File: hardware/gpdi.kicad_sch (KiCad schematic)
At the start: 11 parts, among them J1 GPDI_A, Q1 BSN20, U14 UCL0524P, U15 UCL0524P

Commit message: Initial layout
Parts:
- R21: renamed from R16; value 30k -> 33k; footprint Resistor_SMD:R_0603_1608Metric -> Resistor_SMD:R_0402_1005Metric; LCSC Part # C22984 -> C25779
- R22: renamed from R17; value 30k -> 33k; footprint Resistor_SMD:R_0603_1608Metric -> Resistor_SMD:R_0402_1005Metric; LCSC Part # C22984 -> C25779
- renumbered C15 to C35, D2 to D1, D1 to D2, J1 to J2, R18 to R20, U14 to U4, U15 to U5
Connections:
- net GPDI_GCLK- renamed GPDI_CLK-
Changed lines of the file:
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@@
 		)
 	)
-	(label "GPDI_GCLK-"
+	(label "GPDI_CLK-"
 		(at 114.3 115.57 0)
 		(effects
@@
 		(dnp no)
 		(fields_autoplaced yes)
-		(property "Reference" "D2"
+		(property "Reference" "D1"
 			(at 153.67 37.1474 90)
 			(effects
@@
 			(project "cm0"
 				(path "/b53f5dbb-8078-4818-9e8f-fdf90ba6d854/f05ec484-f958-442a-a016-134b1e35dc2c"
-					(reference "D2")
+					(reference "D1")
 					(unit 1)
 				)
@@
 		(on_board yes)
 		(dnp no)
-		(property "Reference" "U14"
+		(property "Reference" "U4"
 			(at 144.78 78.232 0)
 			(effects
@@
 			(project ""
 				(path "/b53f5dbb-8078-4818-9e8f-fdf90ba6d854/f05ec484-f958-442a-a016-134b1e35dc2c"
-					(reference "U14")
+					(reference "U4")
 					(unit 1)
 				)
@@
 		(on_board yes)
 		(dnp no)
-		(property "Reference" "C15"
+		(property "Reference" "C35"
 			(at 186.69 90.1701 0)
 			(effects
@@
 			(project "cm0"
 				(path "/b53f5dbb-8078-4818-9e8f-fdf90ba6d854/f05ec484-f958-442a-a016-134b1e35dc2c"
-					(reference "C15")
+					(reference "C35")
 					(unit 1)
 				)
@@
 		(on_board yes)
 		(dnp no)
-		(property "Reference" "R17"
+		(property "Reference" "R22"
 			(at 151.13 46.99 90)
 			(effects
@@
 			)
 		)
-		(property "Value" "30k"
+		(property "Value" "33k"
 			(at 153.416 46.99 90)
 			(effects
@@
 			)
 		)
-		(property "Footprint" "Resistor_SMD:R_0603_1608Metric"
+		(property "Footprint" "Resistor_SMD:R_0402_1005Metric"
 			(at 149.352 46.99 90)
 			(effects
@@
 			)
 		)
-		(property "LCSC Part #" "C22984"
+		(property "LCSC Part #" "C25779"
 			(at 151.13 46.99 90)
 			(effects
@@
 			(project "cm0"
 				(path "/b53f5dbb-8078-4818-9e8f-fdf90ba6d854/f05ec484-f958-442a-a016-134b1e35dc2c"
-					(reference "R17")
+					(reference "R22")
 					(unit 1)
 				)
@@
 		(dnp no)
 		(fields_autoplaced yes)
-		(property "Reference" "#PWR070"
+		(property "Reference" "#PWR045"
 			(at 153.67 144.78 0)
 			(effects
@@
 			(project ""
 				(path "/b53f5dbb-8078-4818-9e8f-fdf90ba6d854/f05ec484-f958-442a-a016-134b1e35dc2c"
-					(reference "#PWR070")
+					(reference "#PWR045")
 					(unit 1)
 				)
@@
 		(dnp no)
 		(fields_autoplaced yes)
-		(property "Reference" "#PWR071"
+		(property "Reference" "#PWR042"
 			(at 135.89 144.78 0)
 			(effects
@@
 			(project "cm0"
 				(path "/b53f5dbb-8078-4818-9e8f-fdf90ba6d854/f05ec484-f958-442a-a016-134b1e35dc2c"
-					(reference "#PWR071")
+					(reference "#PWR042")
 					(unit 1)
 				)
@@
 		(dnp no)
 		(fields_autoplaced yes)
-		(property "Reference" "#PWR032"
+		(property "Reference" "#PWR044"
 			(at 151.13 36.83 0)
 			(effects
@@
 			(project "cm0"
 				(path "/b53f5dbb-8078-4818-9e8f-fdf90ba6d854/f05ec484-f958-442a-a016-134b1e35dc2c"
-					(reference "#PWR032")
+					(reference "#PWR044")
 					(unit 1)
 				)
@@
 		(on_board yes)
 		(dnp no)
-		(property "Reference" "#PWR030"
+		(property "Reference" "#PWR048"
 			(at 182.88 100.33 0)
 			(effects
@@
 			(project "cm0"
 				(path "/b53f5dbb-8078-4818-9e8f-fdf90ba6d854/f05ec484-f958-442a-a016-134b1e35dc2c"
-					(reference "#PWR030")
+					(reference "#PWR048")
 					(unit 1)
 				)
@@
 		(dnp no)
 		(fields_autoplaced yes)
-		(property "Reference" "#PWR029"
+		(property "Reference" "#PWR047"
 			(at 168.91 149.86 0)
 			(effects
@@
 			(project ""
 				(path "/b53f5dbb-8078-4818-9e8f-fdf90ba6d854/f05ec484-f958-442a-a016-134b1e35dc2c"
-					(reference "#PWR029")
+					(reference "#PWR047")
 					(unit 1)
 				)
@@
 		(on_board yes)
 		(dnp no)
-		(property "Reference" "R18"
+		(property "Reference" "R20"
 			(at 132.08 77.47 90)
 			(effects
@@
 			(project "cm0"
 				(path "/b53f5dbb-8078-4818-9e8f-fdf90ba6d854/f05ec484-f958-442a-a016-134b1e35dc2c"
-					(reference "R18")
+					(reference "R20")
 					(unit 1)
 				)
@@
 		(dnp no)
 		(fields_autoplaced yes)
-		(property "Reference" "D1"
+		(property "Reference" "D2"
 			(at 170.18 77.7874 90)
 			(effects
@@
 			(project ""
 				(path "/b53f5dbb-8078-4818-9e8f-fdf90ba6d854/f05ec484-f958-442a-a016-134b1e35dc2c"
-					(reference "D1")
+					(reference "D2")
 					(unit 1)
 				)
@@
 		(dnp no)
 		(fields_autoplaced yes)
-		(property "Reference" "#PWR031"
+		(property "Reference" "#PWR043"
 			(at 140.97 36.83 0)
 			(effects
@@
 			(project ""
 				(path "/b53f5dbb-8078-4818-9e8f-fdf90ba6d854/f05ec484-f958-442a-a016-134b1e35dc2c"
-					(reference "#PWR031")
+					(reference "#PWR043")
 					(unit 1)
 				)
@@
 		(on_board yes)
 		(dnp no)
-		(property "Reference" "U15"
+		(property "Reference" "U5"
 			(at 144.78 83.82 0)
 			(effects
@@
 			(project "cm0"
 				(path "/b53f5dbb-8078-4818-9e8f-fdf90ba6d854/f05ec484-f958-442a-a016-134b1e35dc2c"
-					(reference "U15")
+					(reference "U5")
 					(unit 1)
 				)
@@
 		(dnp no)
 		(fields_autoplaced yes)
-		(property "Reference" "J1"
+		(property "Reference" "J2"
 			(at 179.07 111.7599 0)
 			(effects
@@
 			(project ""
 				(path "/b53f5dbb-8078-4818-9e8f-fdf90ba6d854/f05ec484-f958-442a-a016-134b1e35dc2c"
-					(reference "J1")
+					(reference "J2")
 					(unit 1)
 				)
@@
 		(dnp no)
 		(fields_autoplaced yes)
-		(property "Reference" "#PWR028"
+		(property "Reference" "#PWR046"
 			(at 167.64 77.47 0)
 			(effects
@@
 			(project ""
 				(path "/b53f5dbb-8078-4818-9e8f-fdf90ba6d854/f05ec484-f958-442a-a016-134b1e35dc2c"
-					(reference "#PWR028")
+					(reference "#PWR046")
 					(unit 1)
 				)
@@
 		(dnp no)
 		(fields_autoplaced yes)
-		(property "Reference" "#PWR033"
+		(property "Reference" "#PWR041"
 			(at 129.54 74.93 0)
 			(effects
@@
 			(project "cm0"
 				(path "/b53f5dbb-8078-4818-9e8f-fdf90ba6d854/f05ec484-f958-442a-a016-134b1e35dc2c"
-					(reference "#PWR033")
+					(reference "#PWR041")
 					(unit 1)
 				)
@@
 		(on_board yes)
 		(dnp no)
-		(property "Reference" "R16"
+		(property "Reference" "R21"
 			(at 137.16 46.99 90)
 			(effects
@@
 			)
 		)
-		(property "Value" "30k"
+		(property "Value" "33k"
 			(at 139.446 46.99 90)
 			(effects
@@
 			)
 		)
-		(property "Footprint" "Resistor_SMD:R_0603_1608Metric"
+		(property "Footprint" "Resistor_SMD:R_0402_1005Metric"
 			(at 135.382 46.99 90)
 			(effects
@@
 			)
 		)
-		(property "LCSC Part #" "C22984"
+		(property "LCSC Part #" "C25779"
 			(at 137.16 46.99 90)
 			(effects
@@
 			(project "cm0"
 				(path "/b53f5dbb-8078-4818-9e8f-fdf90ba6d854/f05ec484-f958-442a-a016-134b1e35dc2c"
-					(reference "R16")
-					(unit 1)
-				)
+					(reference "R21")
+					(unit 1)
+				)

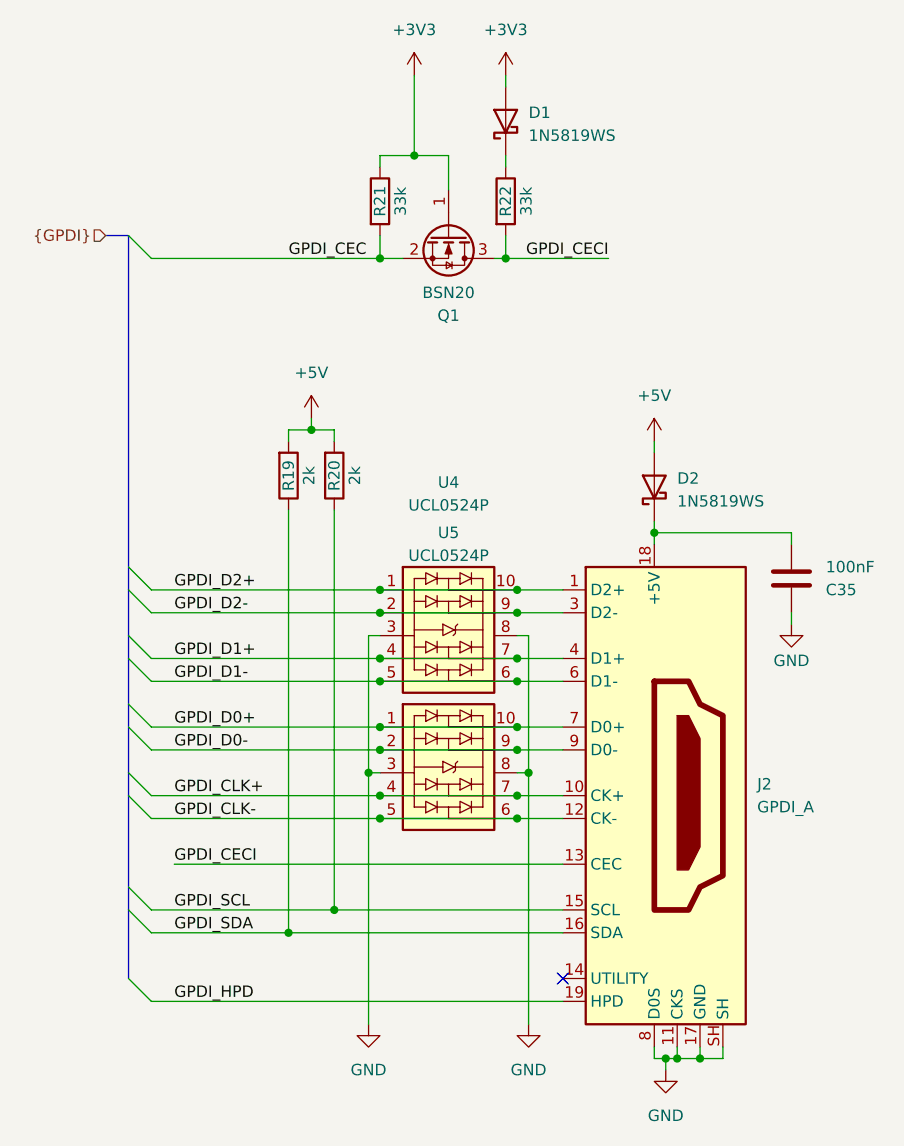
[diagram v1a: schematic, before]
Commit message: Finished DC DC converters and started decoupling the CPU
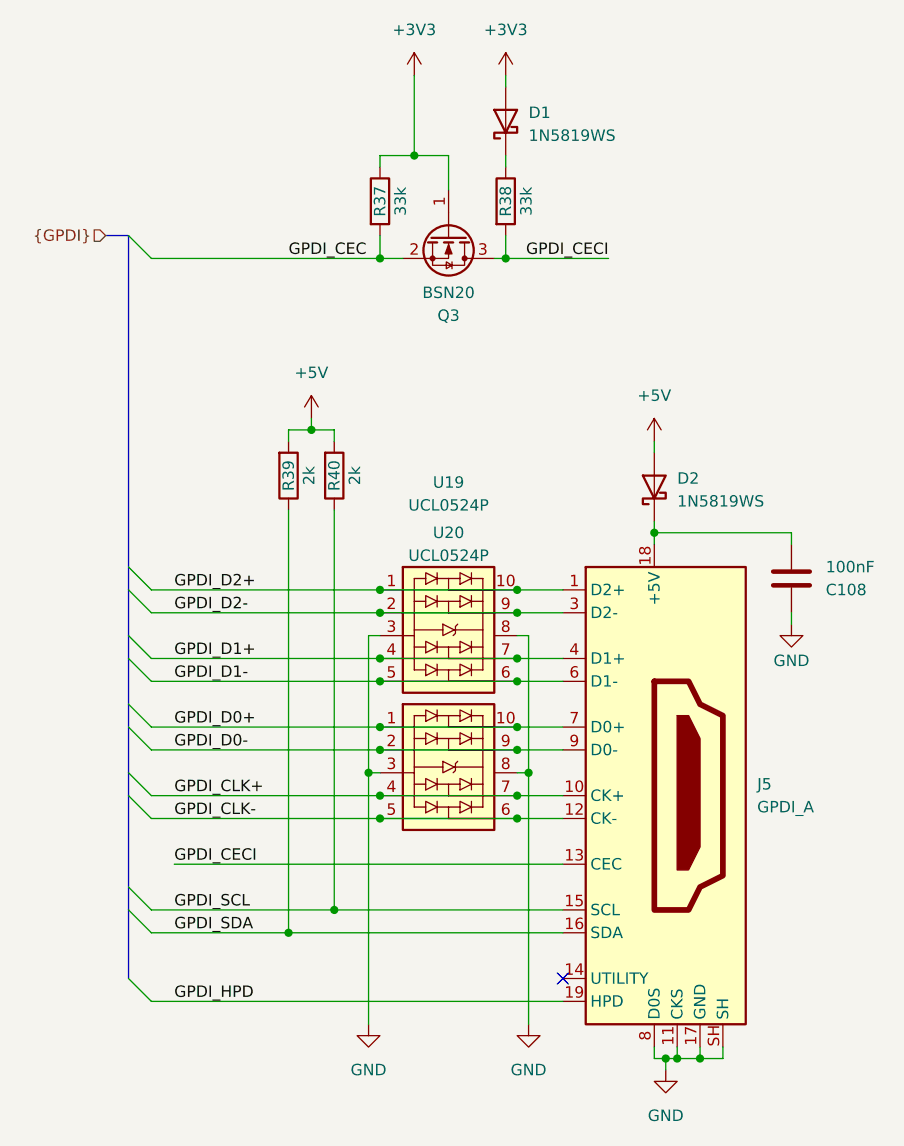
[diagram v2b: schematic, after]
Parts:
- renumbered C35 to C108, J2 to J5, Q1 to Q3, R21 to R37, R22 to R38, R19 to R39, R20 to R40, U4 to U19, U5 to U20
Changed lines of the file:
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@@
 		(on_board yes)
 		(dnp no)
-		(property "Reference" "R19"
+		(property "Reference" "R39"
 			(at 127 77.47 90)
 			(effects
@@
 			(project "cm0"
 				(path "/b53f5dbb-8078-4818-9e8f-fdf90ba6d854/f05ec484-f958-442a-a016-134b1e35dc2c"
-					(reference "R19")
+					(reference "R39")
 					(unit 1)
 				)
@@
 		(on_board yes)
 		(dnp no)
-		(property "Reference" "U4"
+		(property "Reference" "U19"
 			(at 144.78 78.232 0)
 			(effects
@@
 			(project ""
 				(path "/b53f5dbb-8078-4818-9e8f-fdf90ba6d854/f05ec484-f958-442a-a016-134b1e35dc2c"
-					(reference "U4")
+					(reference "U19")
 					(unit 1)
 				)
@@
 		(on_board yes)
 		(dnp no)
-		(property "Reference" "C35"
+		(property "Reference" "C108"
 			(at 186.69 90.1701 0)
 			(effects
@@
 			(project "cm0"
 				(path "/b53f5dbb-8078-4818-9e8f-fdf90ba6d854/f05ec484-f958-442a-a016-134b1e35dc2c"
-					(reference "C35")
+					(reference "C108")
 					(unit 1)
 				)
@@
 		(on_board yes)
 		(dnp no)
-		(property "Reference" "R22"
+		(property "Reference" "R38"
 			(at 151.13 46.99 90)
 			(effects
@@
 			(project "cm0"
 				(path "/b53f5dbb-8078-4818-9e8f-fdf90ba6d854/f05ec484-f958-442a-a016-134b1e35dc2c"
-					(reference "R22")
+					(reference "R38")
 					(unit 1)
 				)
@@
 		(on_board yes)
 		(dnp no)
-		(property "Reference" "Q1"
+		(property "Reference" "Q3"
 			(at 144.78 59.69 90)
 			(effects
@@
 			(project ""
 				(path "/b53f5dbb-8078-4818-9e8f-fdf90ba6d854/f05ec484-f958-442a-a016-134b1e35dc2c"
-					(reference "Q1")
+					(reference "Q3")
 					(unit 1)
 				)
@@
 		(dnp no)
 		(fields_autoplaced yes)
-		(property "Reference" "#PWR045"
+		(property "Reference" "#PWR0127"
 			(at 153.67 144.78 0)
 			(effects
@@
 			(project ""
 				(path "/b53f5dbb-8078-4818-9e8f-fdf90ba6d854/f05ec484-f958-442a-a016-134b1e35dc2c"
-					(reference "#PWR045")
+					(reference "#PWR0127")
 					(unit 1)
 				)
@@
 		(dnp no)
 		(fields_autoplaced yes)
-		(property "Reference" "#PWR042"
+		(property "Reference" "#PWR0126"
 			(at 135.89 144.78 0)
 			(effects
@@
 			(project "cm0"
 				(path "/b53f5dbb-8078-4818-9e8f-fdf90ba6d854/f05ec484-f958-442a-a016-134b1e35dc2c"
-					(reference "#PWR042")
+					(reference "#PWR0126")
 					(unit 1)
 				)
@@
 		(dnp no)
 		(fields_autoplaced yes)
-		(property "Reference" "#PWR044"
+		(property "Reference" "#PWR0122"
 			(at 151.13 36.83 0)
 			(effects
@@
 			(project "cm0"
 				(path "/b53f5dbb-8078-4818-9e8f-fdf90ba6d854/f05ec484-f958-442a-a016-134b1e35dc2c"
-					(reference "#PWR044")
+					(reference "#PWR0122")
 					(unit 1)
 				)
@@
 		(on_board yes)
 		(dnp no)
-		(property "Reference" "#PWR048"
+		(property "Reference" "#PWR0125"
 			(at 182.88 100.33 0)
 			(effects
@@
 			(project "cm0"
 				(path "/b53f5dbb-8078-4818-9e8f-fdf90ba6d854/f05ec484-f958-442a-a016-134b1e35dc2c"
-					(reference "#PWR048")
+					(reference "#PWR0125")
 					(unit 1)
 				)
@@
 		(dnp no)
 		(fields_autoplaced yes)
-		(property "Reference" "#PWR047"
+		(property "Reference" "#PWR0128"
 			(at 168.91 149.86 0)
 			(effects
@@
 			(project ""
 				(path "/b53f5dbb-8078-4818-9e8f-fdf90ba6d854/f05ec484-f958-442a-a016-134b1e35dc2c"
-					(reference "#PWR047")
+					(reference "#PWR0128")
 					(unit 1)
 				)
@@
 		(on_board yes)
 		(dnp no)
-		(property "Reference" "R20"
+		(property "Reference" "R40"
 			(at 132.08 77.47 90)
 			(effects
@@
 			(project "cm0"
 				(path "/b53f5dbb-8078-4818-9e8f-fdf90ba6d854/f05ec484-f958-442a-a016-134b1e35dc2c"
-					(reference "R20")
+					(reference "R40")
 					(unit 1)
 				)
@@
 		(dnp no)
 		(fields_autoplaced yes)
-		(property "Reference" "#PWR043"
+		(property "Reference" "#PWR0121"
 			(at 140.97 36.83 0)
 			(effects
@@
 			(project ""
 				(path "/b53f5dbb-8078-4818-9e8f-fdf90ba6d854/f05ec484-f958-442a-a016-134b1e35dc2c"
-					(reference "#PWR043")
+					(reference "#PWR0121")
 					(unit 1)
 				)
@@
 		(on_board yes)
 		(dnp no)
-		(property "Reference" "U5"
+		(property "Reference" "U20"
 			(at 144.78 83.82 0)
 			(effects
@@
 			(project "cm0"
 				(path "/b53f5dbb-8078-4818-9e8f-fdf90ba6d854/f05ec484-f958-442a-a016-134b1e35dc2c"
-					(reference "U5")
+					(reference "U20")
 					(unit 1)
 				)
@@
 		(dnp no)
 		(fields_autoplaced yes)
-		(property "Reference" "J2"
+		(property "Reference" "J5"
 			(at 179.07 111.7599 0)
 			(effects
@@
 			(project ""
 				(path "/b53f5dbb-8078-4818-9e8f-fdf90ba6d854/f05ec484-f958-442a-a016-134b1e35dc2c"
-					(reference "J2")
+					(reference "J5")
 					(unit 1)
 				)
@@
 		(dnp no)
 		(fields_autoplaced yes)
-		(property "Reference" "#PWR046"
+		(property "Reference" "#PWR0124"
 			(at 167.64 77.47 0)
 			(effects
@@
 			(project ""
 				(path "/b53f5dbb-8078-4818-9e8f-fdf90ba6d854/f05ec484-f958-442a-a016-134b1e35dc2c"
-					(reference "#PWR046")
+					(reference "#PWR0124")
 					(unit 1)
 				)
@@
 		(dnp no)
 		(fields_autoplaced yes)
-		(property "Reference" "#PWR041"
+		(property "Reference" "#PWR0123"
 			(at 129.54 74.93 0)
 			(effects
@@
 			(project "cm0"
 				(path "/b53f5dbb-8078-4818-9e8f-fdf90ba6d854/f05ec484-f958-442a-a016-134b1e35dc2c"
-					(reference "#PWR041")
+					(reference "#PWR0123")
 					(unit 1)
 				)
@@
 		(on_board yes)
 		(dnp no)
-		(property "Reference" "R21"
+		(property "Reference" "R37"
 			(at 137.16 46.99 90)
 			(effects
@@
 			(project "cm0"
 				(path "/b53f5dbb-8078-4818-9e8f-fdf90ba6d854/f05ec484-f958-442a-a016-134b1e35dc2c"
-					(reference "R21")
-					(unit 1)
-				)
+					(reference "R37")
+					(unit 1)
+				)

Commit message: Decoupling on PCB side almost done
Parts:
- added U23: UCL0524P, Package_DFN_QFN:Diodes_UDFN-10_1.0x2.5mm_P0.5mm, symbol cm0:UCL0524P
- U19, U20: FT Rotation Offset (none) -> -90
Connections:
- net D1S: now also U23.3, U23.8
- net GPDI_CECI: now also U23.1, U23.10
- net GPDI_HPD: now also U23.5, U23.6
- net GPDI_SCL: now also U23.2, U23.9
- net GPDI_SDA: now also U23.4, U23.7
